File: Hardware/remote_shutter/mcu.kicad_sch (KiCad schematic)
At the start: 1 part

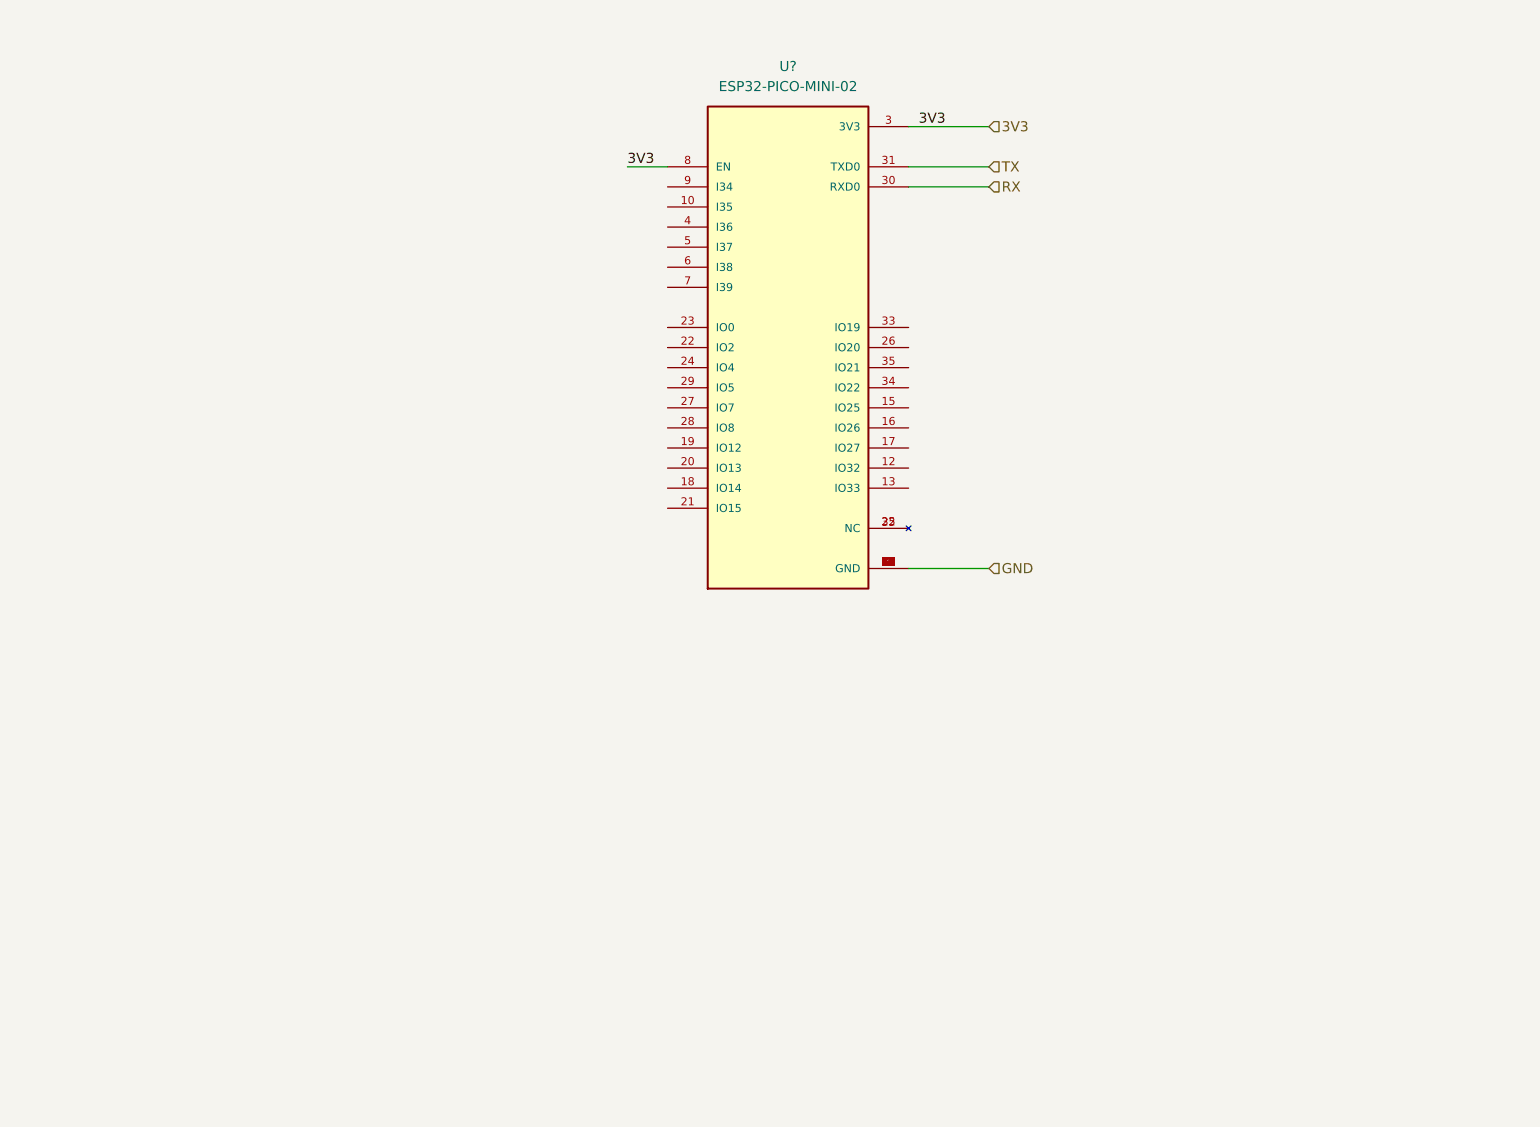
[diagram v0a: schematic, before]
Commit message: Added BOM. Added controls.
Placed jack, switches, OLED display and rotary encoders.
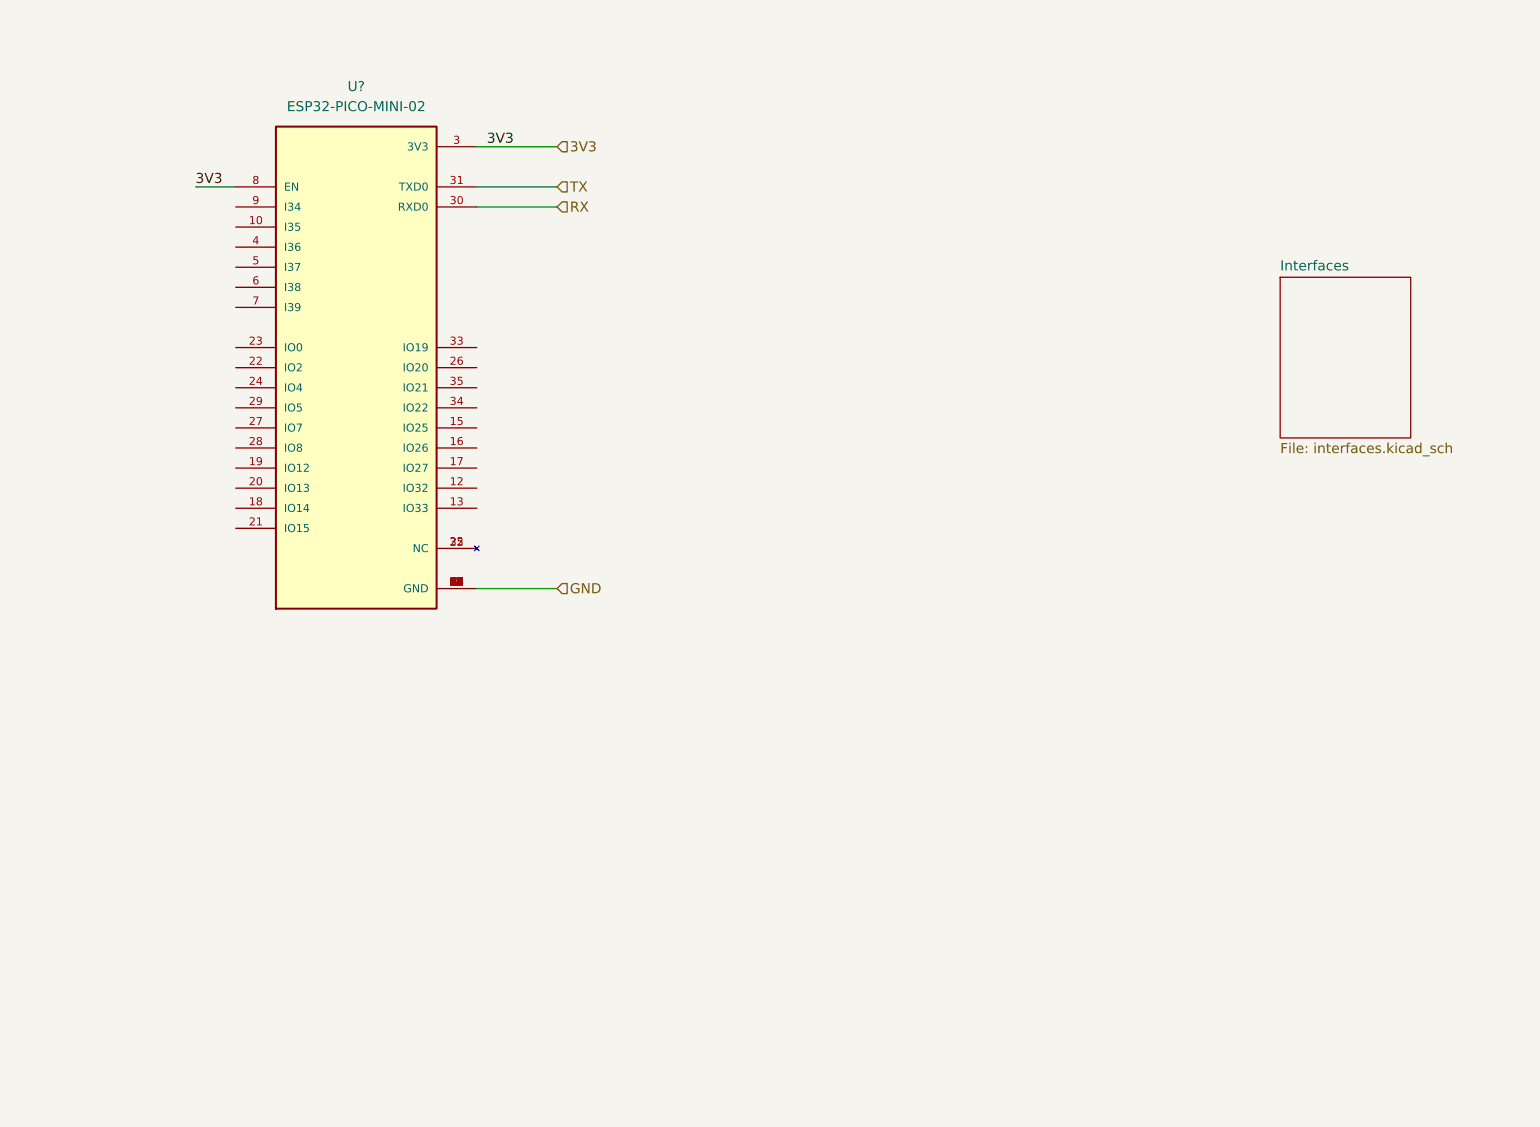
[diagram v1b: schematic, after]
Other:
- added sheet Interfaces (interfaces.kicad_sch)
- moved on the sheet: U?
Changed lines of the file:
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@@
 (kicad_sch (version 20211123) (generator eeschema)
   (paper "A4")
-  (wire (pts (xy 162.56 58.42) (xy 172.72 58.42))
+  (wire (pts (xy 107.95 60.96) (xy 118.11 60.96))
     (stroke (width 0) (type default) (color 0 0 0 0))
   )
-  (wire (pts (xy 162.56 60.96) (xy 172.72 60.96))
+  (wire (pts (xy 107.95 63.5) (xy 118.11 63.5))
     (stroke (width 0) (type default) (color 0 0 0 0))
   )
-  (wire (pts (xy 127 58.42) (xy 132.08 58.42))
+  (wire (pts (xy 72.39 60.96) (xy 77.47 60.96))
     (stroke (width 0) (type default) (color 0 0 0 0))
   )
-  (wire (pts (xy 162.56 53.34) (xy 172.72 53.34))
+  (wire (pts (xy 107.95 55.88) (xy 118.11 55.88))
     (stroke (width 0) (type default) (color 0 0 0 0))
   )
-  (wire (pts (xy 162.56 109.22) (xy 172.72 109.22))
+  (wire (pts (xy 107.95 111.76) (xy 118.11 111.76))
     (stroke (width 0) (type default) (color 0 0 0 0))
   )
-  (label "3V3" (at 127 58.42 0)
+  (label "3V3" (at 72.39 60.96 0)
     (effects (font (size 1.27 1.27)) (justify left bottom))
   )
-  (label "3V3" (at 163.83 53.34 0)
+  (label "3V3" (at 109.22 55.88 0)
     (effects (font (size 1.27 1.27)) (justify left bottom))
   )
-  (hierarchical_label "TX" (shape input) (at 172.72 58.42 0)
+  (hierarchical_label "TX" (shape input) (at 118.11 60.96 0)
     (effects (font (size 1.27 1.27)) (justify left))
   )
-  (hierarchical_label "3V3" (shape input) (at 172.72 53.34 0)
+  (hierarchical_label "3V3" (shape input) (at 118.11 55.88 0)
     (effects (font (size 1.27 1.27)) (justify left))
   )
-  (hierarchical_label "GND" (shape input) (at 172.72 109.22 0)
+  (hierarchical_label "GND" (shape input) (at 118.11 111.76 0)
     (effects (font (size 1.27 1.27)) (justify left))
   )
-  (hierarchical_label "RX" (shape input) (at 172.72 60.96 0)
+  (hierarchical_label "RX" (shape input) (at 118.11 63.5 0)
     (effects (font (size 1.27 1.27)) (justify left))
   )
-  (symbol (lib_id "ESP32-PICO-MINI-02:ESP32-PICO-MINI-02") (at 147.32 81.28 0) (unit 1)
+  (symbol (lib_id "ESP32-PICO-MINI-02:ESP32-PICO-MINI-02") (at 92.71 83.82 0) (unit 1)
     (in_bom yes) (on_board yes) (fields_autoplaced)
-    (property "Reference" "U?" (id 0) (at 147.32 45.72 0))
-    (property "Value" "ESP32-PICO-MINI-02" (id 1) (at 147.32 48.26 0))
-    (property "Footprint" "MODULE_ESP32-PICO-MINI-02" (id 2) (at 147.32 81.28 0)
+    (property "Reference" "U?" (id 0) (at 92.71 48.26 0))
+    (property "Value" "ESP32-PICO-MINI-02" (id 1) (at 92.71 50.8 0))
+    (property "Footprint" "MODULE_ESP32-PICO-MINI-02" (id 2) (at 92.71 83.82 0)
       (effects (font (size 1.27 1.27)) (justify bottom) hide)
     )
-    (property "Datasheet" "" (id 3) (at 147.32 81.28 0)
+    (property "Datasheet" "" (id 3) (at 92.71 83.82 0)
       (effects (font (size 1.27 1.27)) hide)
     )
-    (property "MAXIMUM_PACKAGE_HEIGHT" "2.55mm" (id 4) (at 147.32 81.28 0)
+    (property "MAXIMUM_PACKAGE_HEIGHT" "2.55mm" (id 4) (at 92.71 83.82 0)
       (effects (font (size 1.27 1.27)) (justify bottom) hide)
     )
-    (property "MANUFACTURER" "Espressif" (id 5) (at 147.32 81.28 0)
+    (property "MANUFACTURER" "Espressif" (id 5) (at 92.71 83.82 0)
       (effects (font (size 1.27 1.27)) (justify bottom) hide)
     )
-    (property "PARTREV" "v1.0" (id 6) (at 147.32 81.28 0)
+    (property "PARTREV" "v1.0" (id 6) (at 92.71 83.82 0)
       (effects (font (size 1.27 1.27)) (justify bottom) hide)
     )
-    (property "STANDARD" "Manufacturer Recommendations" (id 7) (at 147.32 81.28 0)
+    (property "STANDARD" "Manufacturer Recommendations" (id 7) (at 92.71 83.82 0)
       (effects (font (size 1.27 1.27)) (justify bottom) hide)
     )
@@
     (pin "9")
   )
+  (sheet (at 209.55 72.39) (size 16.51 20.32) (fields_autoplaced)
+    (stroke (width 0.1524) (type solid) (color 0 0 0 0))
+    (fill (color 255 229 191 1.0000))
+    (property "Sheet name" "Interfaces" (id 0) (at 209.55 71.6784 0)
+      (effects (font (size 1.27 1.27)) (justify left bottom))
+    )
+    (property "Sheet file" "interfaces.kicad_sch" (id 1) (at 209.55 93.2946 0)
+      (effects (font (size 1.27 1.27)) (justify left top))
+    )
+  )
 )

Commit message: Added power & comms.
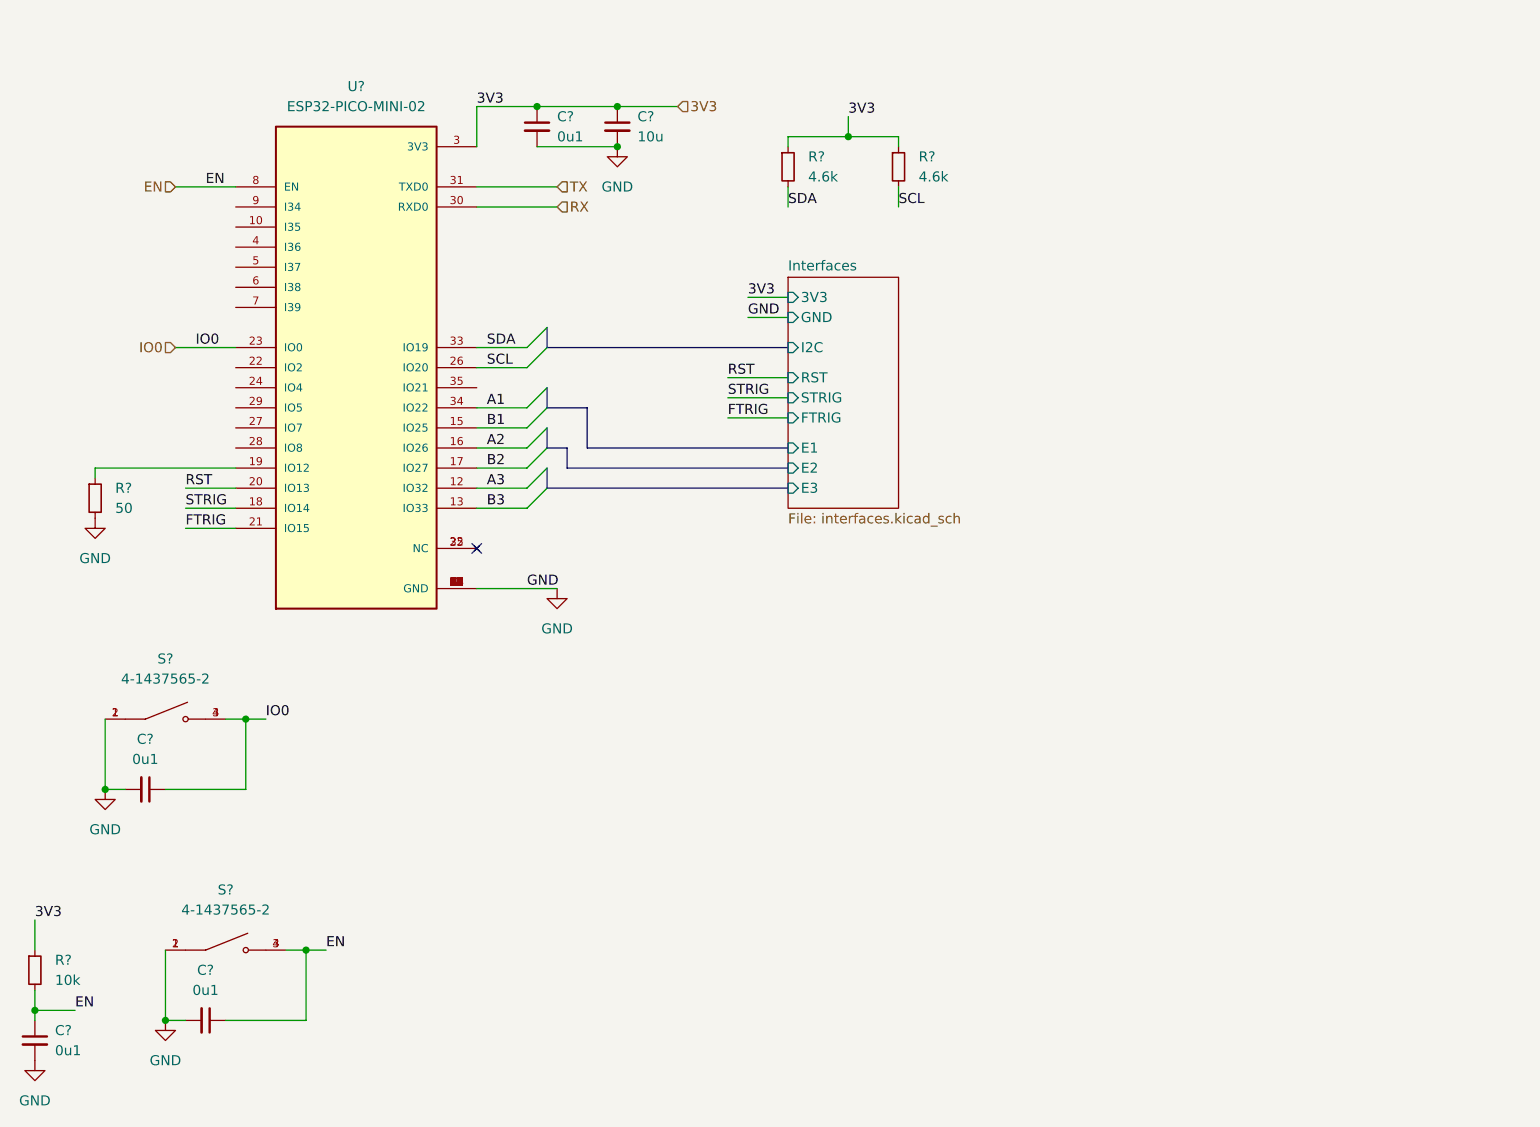
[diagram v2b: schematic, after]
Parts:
- added C? (x4): 0u1, symbol Device:C_Small
- added C?: 10u, symbol Device:C_Small
- added R?: 4.6k, Resistor_SMD:R_0603_1608Metric_Pad0.98x0.95mm_HandSolder, symbol Device:R_Small
- added R?: 50, Resistor_SMD:R_0603_1608Metric_Pad0.98x0.95mm_HandSolder, symbol Device:R_Small
- added R?: 10k, Resistor_SMD:R_0603_1608Metric_Pad0.98x0.95mm_HandSolder, symbol Device:R_Small
- added R?: 4.6k, symbol Device:R_Small
- added S? (x2): 4-1437565-2, SW_4-1437565-2, symbol 4-1437565-2:4-1437565-2
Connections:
- net 3V3: now also C?.1, C?.1, R?.1, R?.1, R?.1; no longer U?.8 (EN)
- net GND: now also C?.2, C?.2, C?.2, C?.2, C?.2, R?.2, S?.1, S?.1, S?.2, S?.2
- net A3: now reaches U?.12 (IO32)
- net B3: now reaches U?.13 (IO33)
- net B1: now reaches U?.15 (IO25)
- net A2: now reaches U?.16 (IO26)
- net B2: now reaches U?.17 (IO27)
- net STRIG: now reaches U?.18 (IO14)
- net at U?.19 (IO12): now also R?.1
- net RST: now reaches U?.20 (IO13)
- net FTRIG: now reaches U?.21 (IO15)
- net IO0: now reaches U?.23 (IO0)
- net IO0: now also C?.1, S?.3, S?.4
- net SCL: now reaches U?.26 (IO20)
- net SCL: now also R?.2
- net SDA: now reaches U?.33 (IO19)
- net SDA: now also R?.2
- net A1: now reaches U?.34 (IO22)
- new net EN: C?.1, C?.1, R?.2, S?.3, S?.4, U?.8 (EN)
- no-connect marks 0 -> 1
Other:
- sheet Interfaces ports: added 3V3, E1, E2, E3, FTRIG, GND, I2C, RST, STRIG; removed none

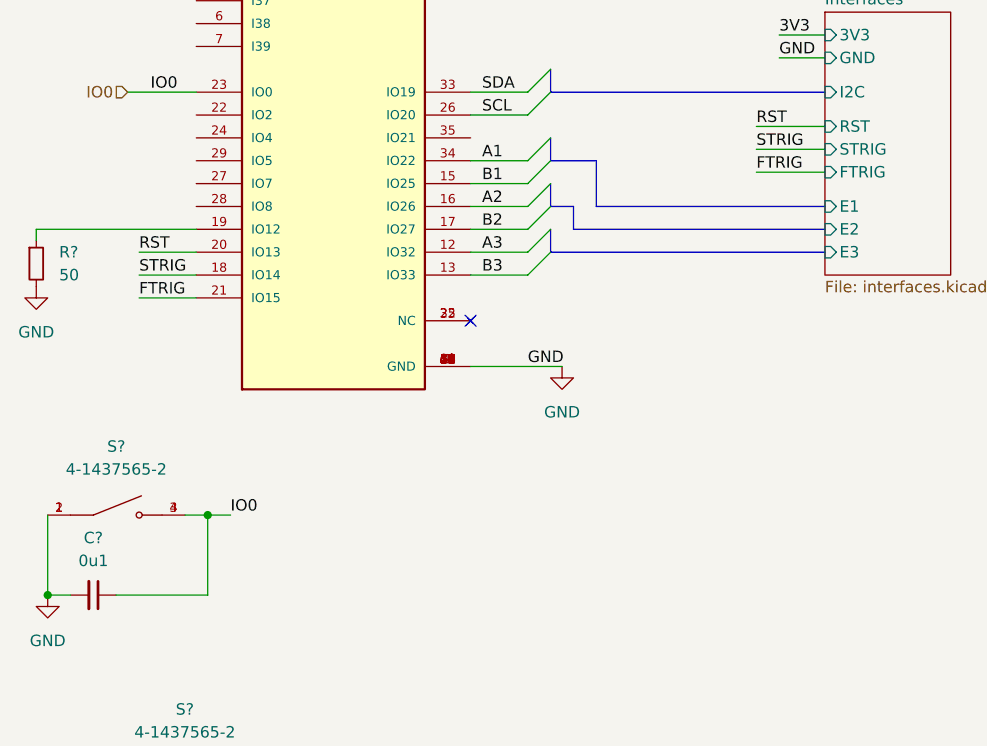
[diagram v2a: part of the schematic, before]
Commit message: Added crystal
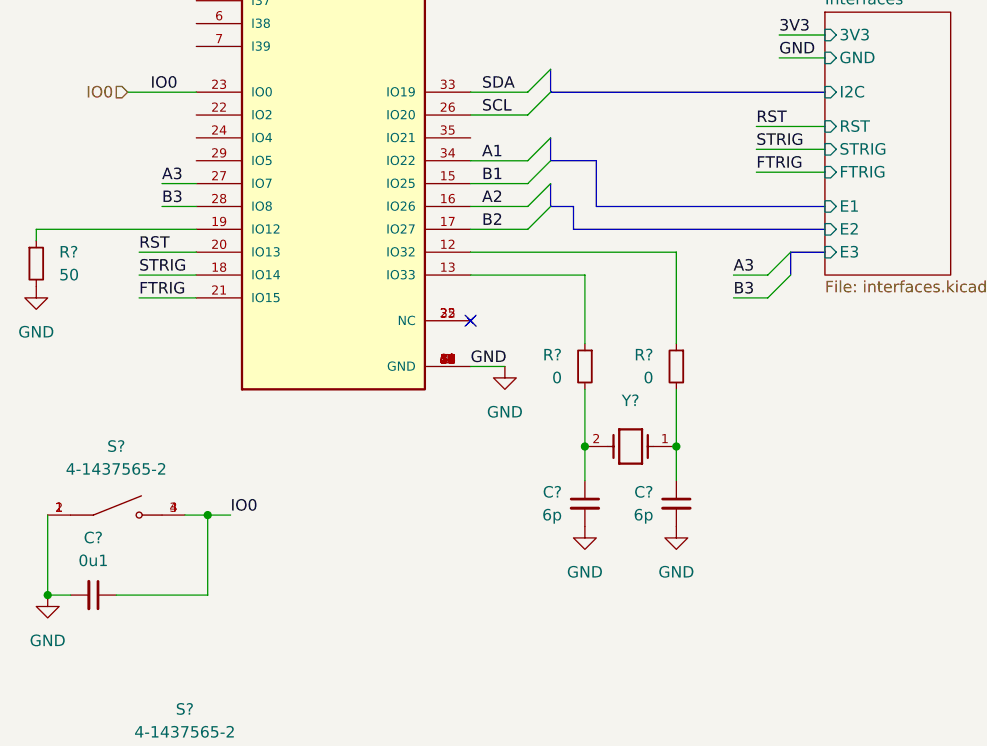
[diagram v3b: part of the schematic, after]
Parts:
- added C? (x2): 6p, Capacitor_SMD:C_0603_1608Metric_Pad1.08x0.95mm_HandSolder, symbol Device:C_Small
- added R? (x2): 0, Resistor_SMD:R_0603_1608Metric_Pad0.98x0.95mm_HandSolder, symbol Device:R_Small
- added Y?: NX3215SA-32.768K-STD-MUA-14, XTAL_NX3215SA-32.768K-STD-MUA-14, symbol NX3215SA-32.768K-STD-MUA-14:NX3215SA-32.768K-STD-MUA-14
- C?: footprint (none) -> Capacitor_SMD:C_0603_1608Metric_Pad1.08x0.95mm_HandSolder
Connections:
- net A3: now also U?.27 (IO7); no longer U?.12 (IO32)
- net B3: now also U?.28 (IO8); no longer U?.13 (IO33)
- net GND: now also C?.2, C?.2
- new net: C?.1, R?.2, Y?.2
- new net: C?.1, R?.2, Y?.1
- new net: R?.1, U?.12 (IO32)
- new net: R?.1, U?.13 (IO33)
